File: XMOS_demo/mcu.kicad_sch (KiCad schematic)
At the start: 53 parts, among them J1 XSYS2 DEBUG CONNECTOR, U1 U316-1024-QF60B, U2 W25Q32JVSS, Y1 Crystal_24M

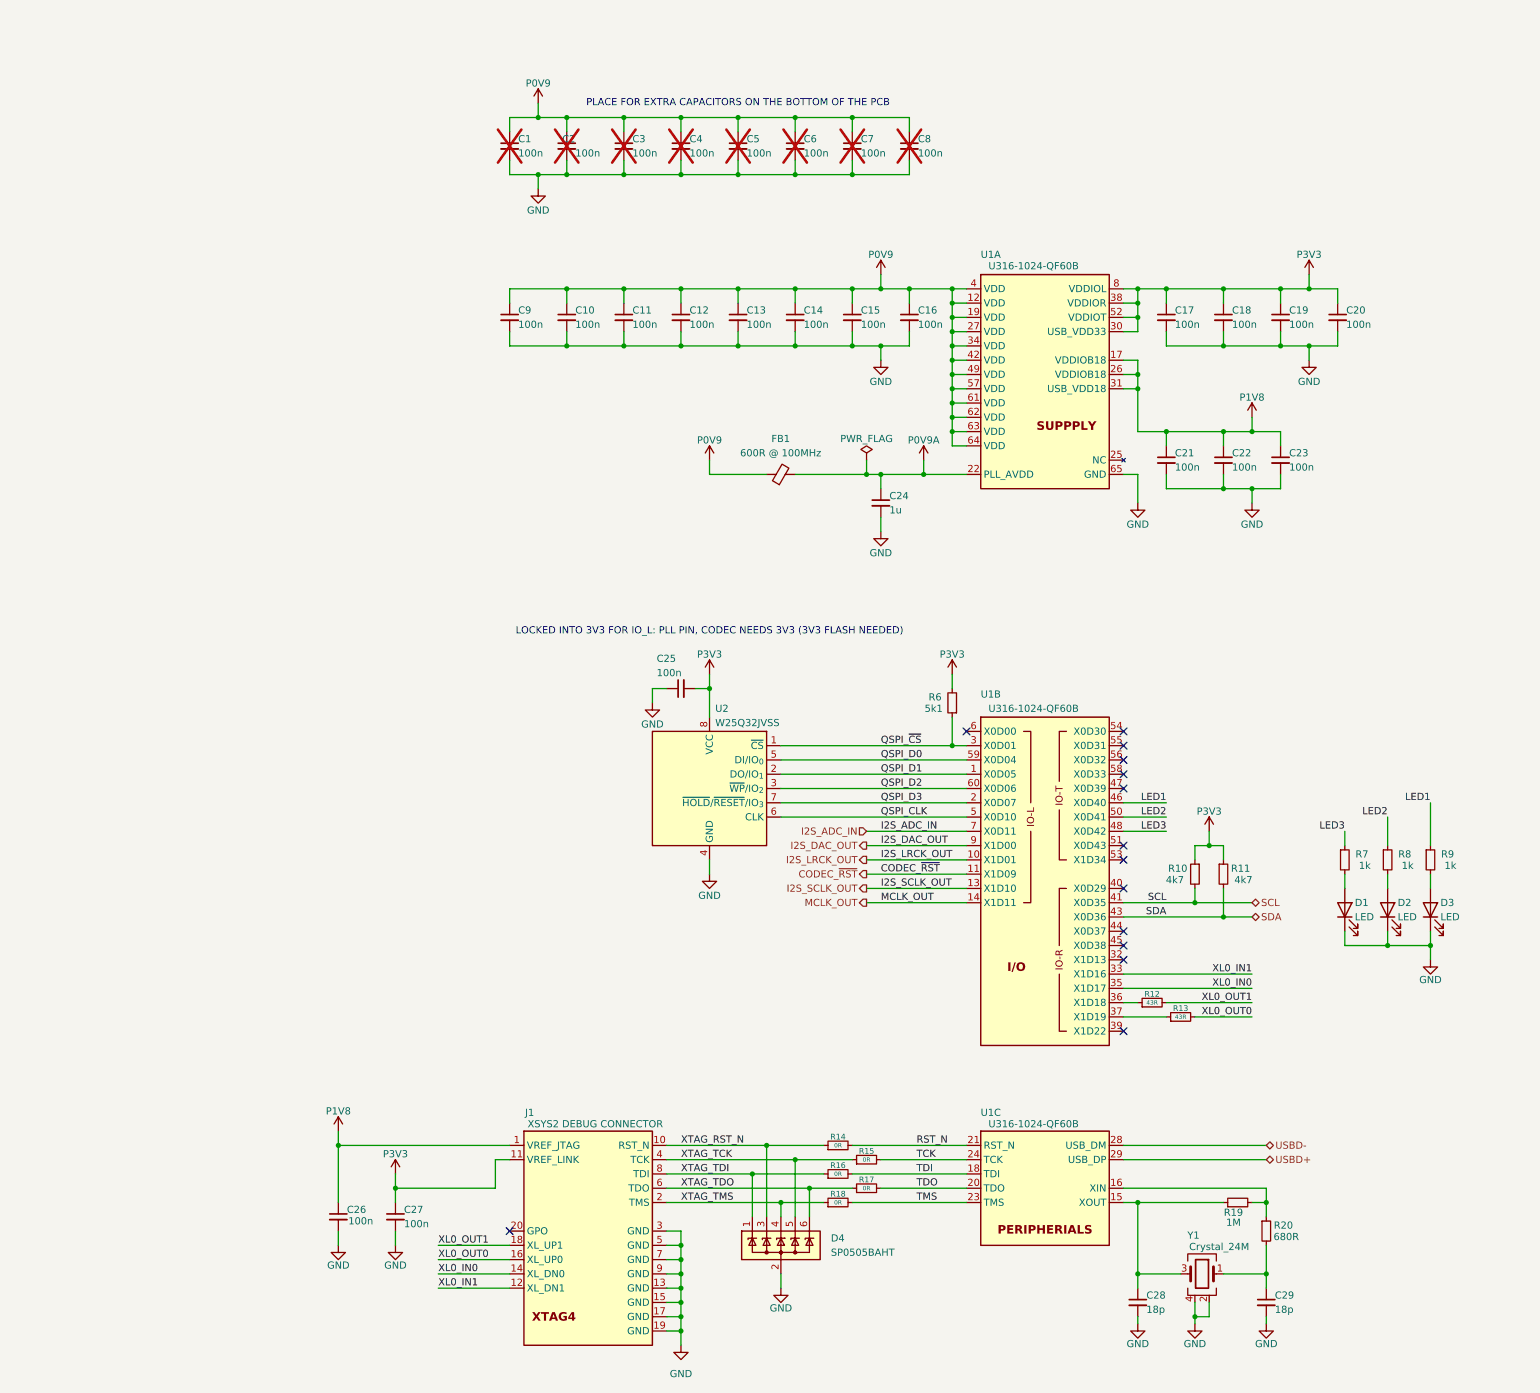
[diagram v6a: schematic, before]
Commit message: Started changes on power supply (audio in) on schematic
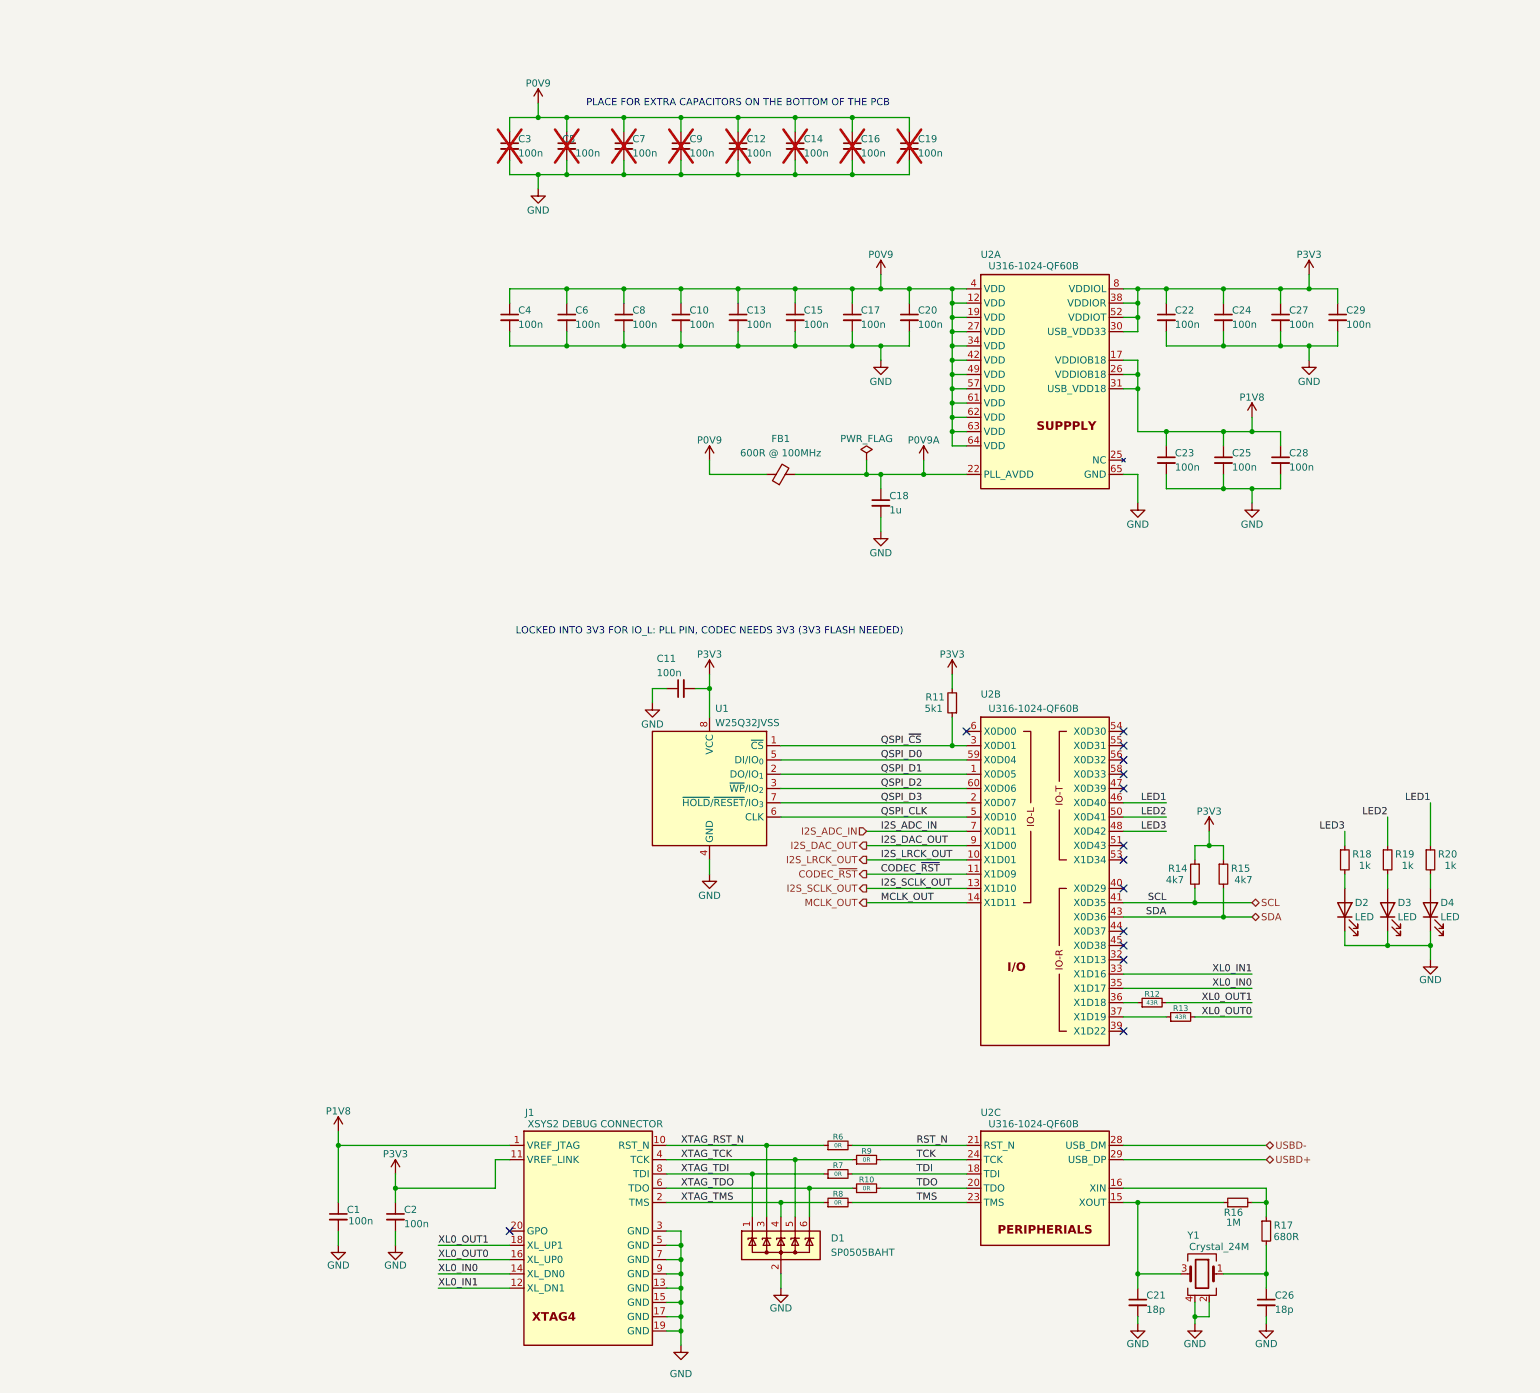
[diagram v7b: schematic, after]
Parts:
- renumbered C26 to C1, C12 to C10, C25 to C11, C5 to C12, C6 to C14, C14 to C15, C7 to C16, C15 to C17, C24 to C18, C8 to C19, C27 to C2, C16 to C20, C28 to C21, C17 to C22, C21 to C23, C18 to C24, C22 to C25, C29 to C26, C19 to C27, C23 to C28, C20 to C29, C1 to C3, C9 to C4, C2 to C5, C10 to C6, C3 to C7, C11 to C8, C4 to C9, D4 to D1, D1 to D2, D2 to D3, D3 to D4, R17 to R10, R6 to R11, R10 to R14, R11 to R15, R19 to R16, R20 to R17, R7 to R18, R8 to R19, R9 to R20, R14 to R6, R16 to R7, R18 to R8, R15 to R9, U2 to U1, U1 to U2

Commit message: Passive lpf added to autio output
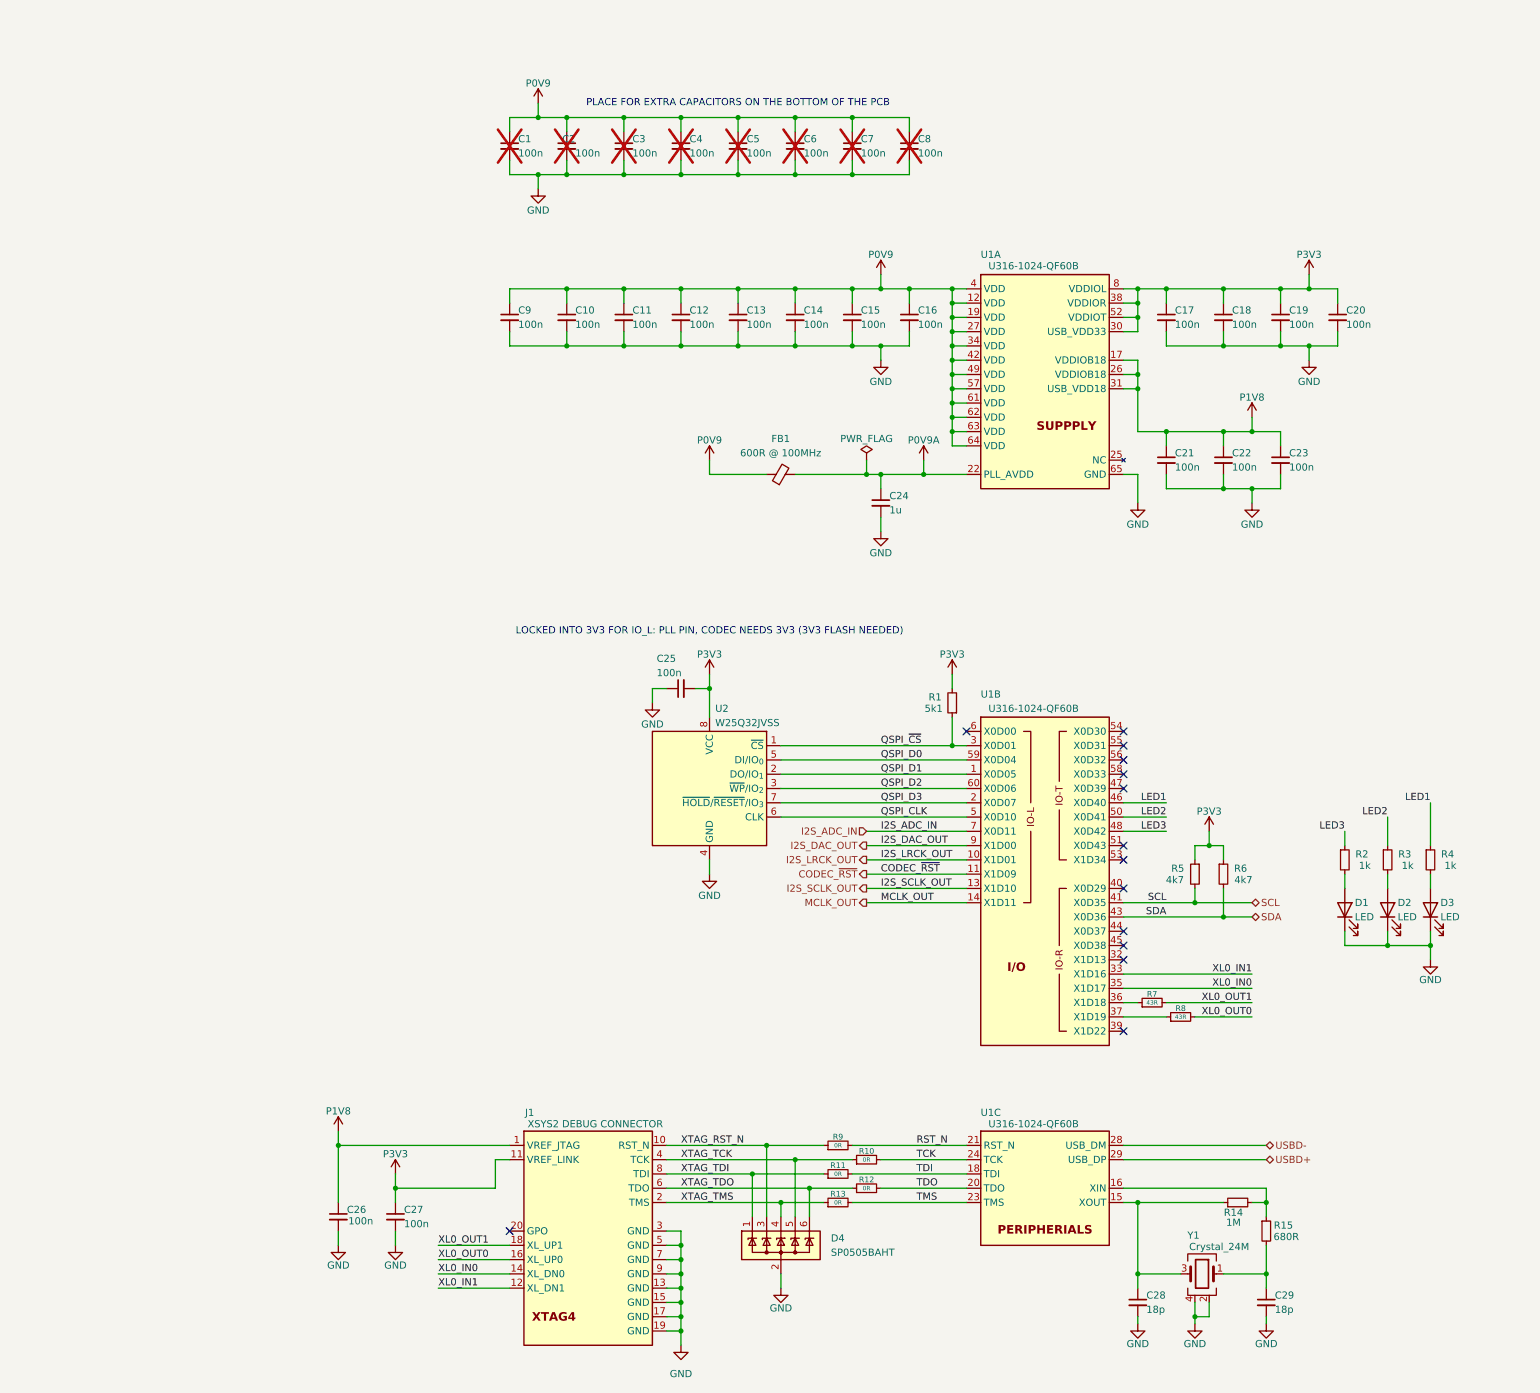
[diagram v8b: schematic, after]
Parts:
- renumbered C3 to C1, C6 to C10, C8 to C11, C10 to C12, C15 to C14, C17 to C15, C20 to C16, C22 to C17, C24 to C18, C27 to C19, C5 to C2, C29 to C20, C23 to C21, C25 to C22, C28 to C23, C18 to C24, C11 to C25, C1 to C26, C2 to C27, C21 to C28, C26 to C29, C7 to C3, C9 to C4, C12 to C5, C14 to C6, C16 to C7, C19 to C8, C4 to C9, D2 to D1, D3 to D2, D4 to D3, D1 to D4, R11 to R1, R9 to R10, R7 to R11, R10 to R12, R8 to R13, R16 to R14, R17 to R15, R18 to R2, R19 to R3, R20 to R4, R14 to R5, R15 to R6, R12 to R7, R13 to R8, R6 to R9, U2 to U1, U1 to U2
